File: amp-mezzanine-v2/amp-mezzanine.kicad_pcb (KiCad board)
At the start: 4 copper layers, 49 x 54.8 mm, 10 parts, among them J1 CTRL, J2 PWR, J3 ONEWIRE, J4 ONEWIRE

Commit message: Updated mezannine v2
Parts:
- added H2: MountingHole_Pad, MountingHole:MountingHole_3.2mm_M3_Pad_Via, F.Cu at (115.0, 96.0)
- J3, J4: value ONEWIRE -> Conn_01x02_MountingPin
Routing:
- net GND: vias 79 -> 76
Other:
- board text added: "Designer: ${DESIGNER} Reviewer: ${REVIEWER} ${COMPANY}"

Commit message: Updated all boards for production
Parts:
- removed A100: R, Jumper:SolderJumper-3_P1.3mm_Open_RoundedPad1.0x1.5mm
- removed A101: NC, Jumper:SolderJumper-3_P1.3mm_Open_RoundedPad1.0x1.5mm
- added H3: ~, MountingHole:MountingHole_3.2mm_M3_Pad_Via, F.Cu at (74.2, 49.1)
- added H4: ~, MountingHole:MountingHole_3.2mm_M3_Pad_Via, F.Cu at (115.0, 80.6)
- H1, H2: value MountingHole_Pad -> ~
- J1, J2: footprint Connector_Molex:Molex_PicoBlade_53261-0971_1x09-1MP_P1.25mm_Horizontal -> Connector_Molex:Molex_PicoBlade_53261-1071_1x10-1MP_P1.25mm_Horizontal
- J3, J4: value Conn_01x02_MountingPin -> ONEWIRE
- moved H2 46.9 mm to (115.0, 49.1)
- moved H1 15.4 mm to (74.2, 80.6)
- moved J1 4.34 mm to (94.7, 91.7)
- moved R1 3.64 mm to (91.9, 86.4)
- moved R2 3.64 mm to (91.9, 84.4)
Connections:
- J1 pad 2: /SDA -> /A1
- J1 pad 4: /CTRL_D -> /SDA
- J1 pad 5: /CTRL_C -> /CTRL_D
- J1 pad 6: /CTRL_B -> /CTRL_C
- J1 pad 7: /CTRL_A -> /CTRL_B
- J1 pad 8: /EN -> /CTRL_A
- J1 pad 9: +3V3 -> /EN
- J2 pad 5: unconnected-(J2-Pin_5-Pad5) -> Vdrive
- R1 pad 1: /SDA -> /SCL
- R2 pad 1: /SCL -> /SDA
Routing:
- net /CTRL_D: track 25.8 -> 11.2 mm
- net /CTRL_C: track 25.4 -> 10.8 mm
- net /CTRL_B: track 25.0 -> 11.0 mm
- net /CTRL_A: track 24.6 -> 11.3 mm
- net /SCL: track 18.3 -> 11.8 mm
- net /SDA: track 16.4 -> 11.9 mm, vias 2 -> 0
- net +3V3: track 21.4 -> 17.3 mm
- net /EN: track 31.1 -> 28.1 mm
- net /A1: track 13.2 -> 11.4 mm, vias 3 -> 0
- net GND: vias 76 -> 66
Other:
- board size 49 x 54.8 mm -> 49 x 50 mm
- board text added: "PIC-D HTR MZN V2 Rev.${BOARD_REV}"

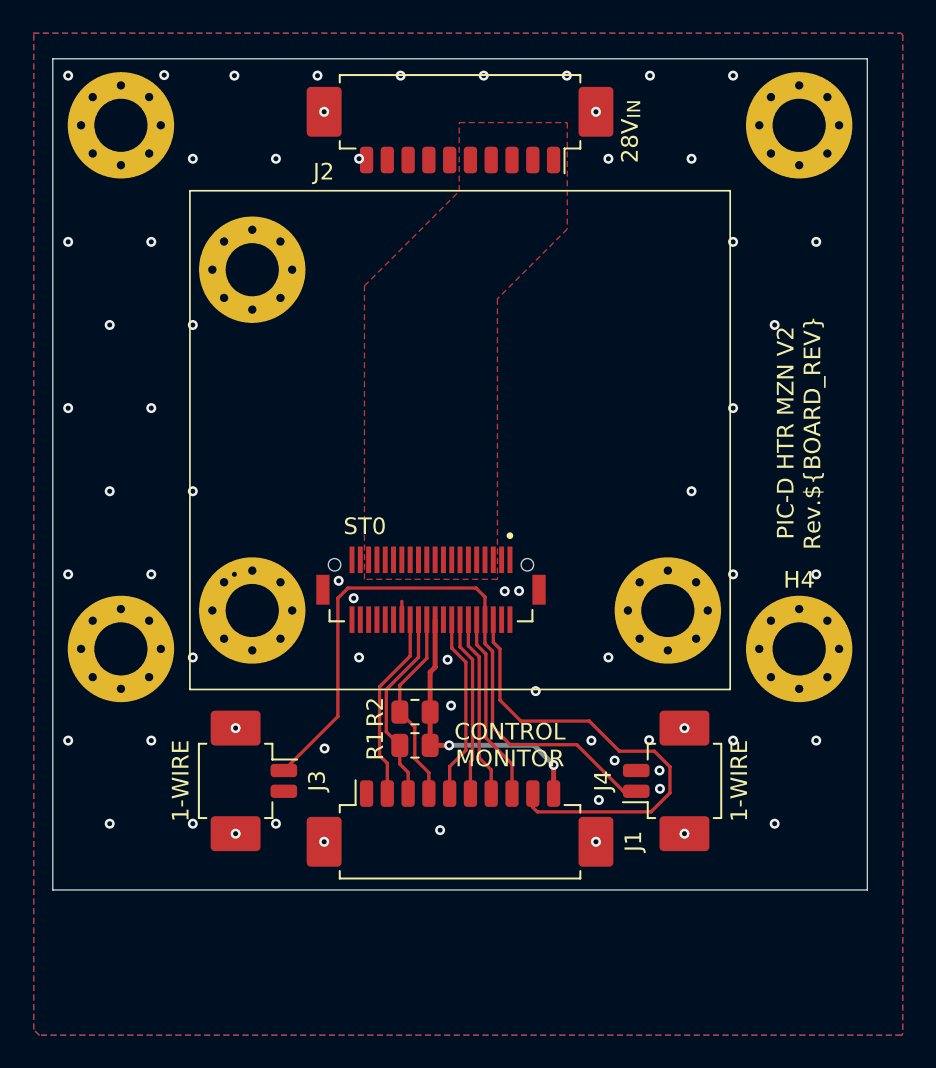
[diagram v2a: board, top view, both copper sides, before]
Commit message: Updated mezzanine v2 with Jason & Joe's comments
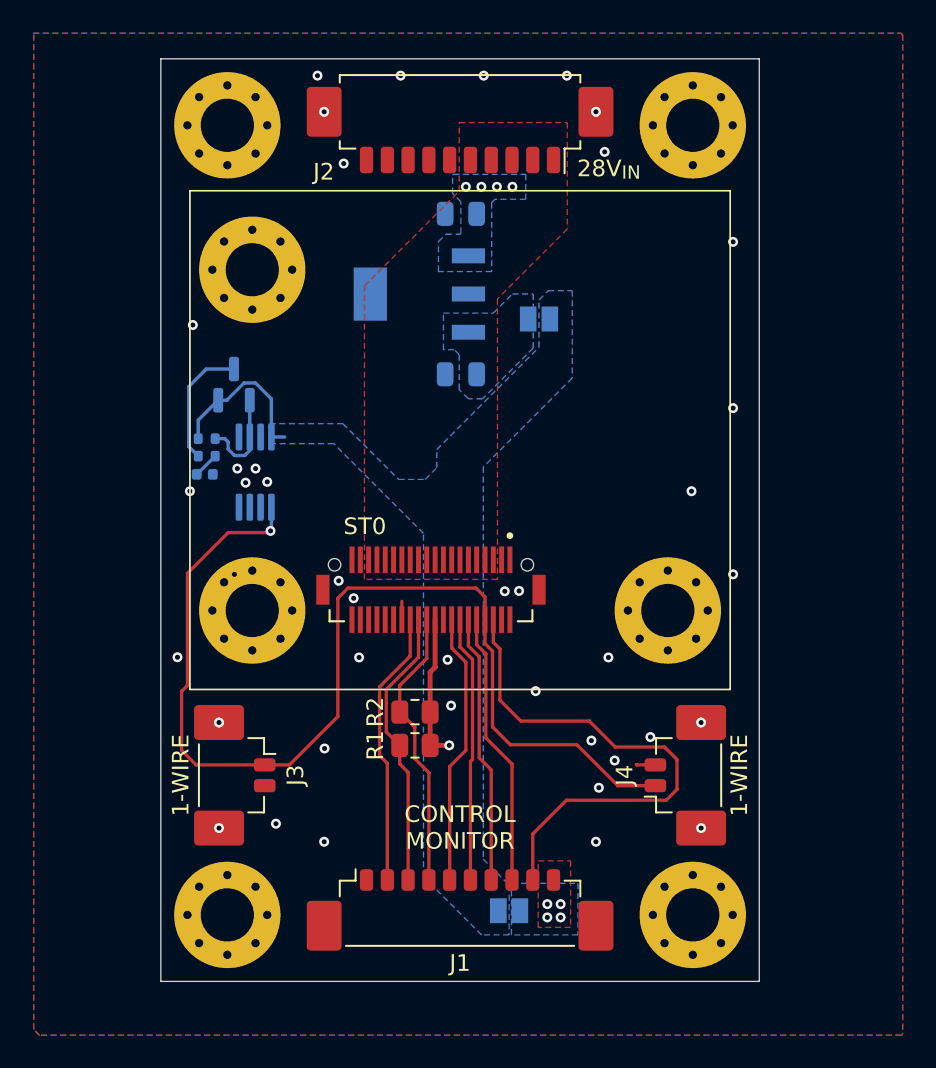
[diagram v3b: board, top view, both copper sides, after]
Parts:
- added C1: 2.2u, Capacitor_SMD:C_0805_2012Metric, B.Cu at (94.7, 54.4)
- added C3: 4.7u, Capacitor_SMD:C_0805_2012Metric, B.Cu at (94.7, 64.0)
- added D1: LED, LED_SMD:LED_0402_1005Metric, B.Cu at (79.3, 70.1)
- added JP1: 3V3_LDO, Jumper:SolderJumper-2_P1.3mm_Open_Pad1.0x1.5mm, B.Cu at (99.4, 60.7)
- added JP2: 3V3_EXT, Jumper:SolderJumper-2_P1.3mm_Open_Pad1.0x1.5mm, B.Cu at (97.6, 96.3)
- added Q1: BSS84, Package_TO_SOT_SMD:SOT-23, B.Cu at (81.0, 64.7)
- added R3: 100k, Resistor_SMD:R_0402_1005Metric, B.Cu at (79.4, 67.9)
- added R4: 1k, Resistor_SMD:R_0402_1005Metric, B.Cu at (79.4, 69.0)
- added U1: DS28EA00, Package_SO:MSOP-8_3x3mm_P0.65mm, B.Cu at (82.3, 69.9)
- added U2: BD433M2FP3-CE2, project_footprints:SOT230P700X180-4N, B.Cu at (92.2, 59.2)
- J1: footprint Connector_Molex:Molex_PicoBlade_53261-1071_1x10-1MP_P1.25mm_Horizontal -> Connector_Molex:Molex_PicoBlade_53398-1071_1x10-1MP_P1.25mm_Vertical
- J3, J4: footprint Connector_Molex:Molex_PicoBlade_53261-0271_1x02-1MP_P1.25mm_Horizontal -> Connector_Molex:Molex_PicoBlade_53398-0271_1x02-1MP_P1.25mm_Vertical
- moved H1 17.2 mm to (80.7, 96.6)
- moved H4 17.2 mm to (108.7, 96.6)
- moved H3 6.40 mm to (80.7, 49.1)
- moved H2 6.40 mm to (108.7, 49.1)
- moved J1 4.05 mm to (94.7, 95.7)
- moved J3 0.34 mm to (81.7, 88.2)
- moved J4 0.34 mm to (107.7, 88.2)
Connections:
- J1 pad 10: +3V3 -> /3V3_IN
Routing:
- net /ONEWIRE: track 39.3 -> 65.0 mm, vias 0 -> 1
- net Net-(Q1-D): track 0.00 -> 7.65 mm
- net /LED_CTRL: track 0.00 -> 5.90 mm
- net /CTRL_B: track 11.0 -> 16.2 mm
- net /CTRL_D: track 11.2 -> 16.4 mm
- net /CTRL_C: track 10.8 -> 16.0 mm
- net /CTRL_A: track 11.3 -> 16.5 mm
- net /A1: track 11.4 -> 16.6 mm
- net /SDA: track 11.9 -> 17.1 mm
- net /SCL: track 11.8 -> 17.0 mm
- net /EN: track 28.1 -> 31.5 mm
- net Net-(D1-A): track 0.00 -> 1.70 mm
- net +3V3: track 17.3 -> 18.8 mm, vias 2 -> 1
- net GND: track 1.10 -> 2.26 mm, vias 66 -> 41
- net Vdrive: vias 0 -> 4
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- added copper zone on B.Cu, net +3V3
- added copper zone on B.Cu, net /3V3_IN
- added copper zone on F.Cu, net /3V3_IN
- added copper zone on B.Cu, net /3V3_LDO
- added copper zone on B.Cu, net Vdrive
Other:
- board size 49 x 50 mm -> 36 x 55.5 mm
- board text added: "3V3_EXT"
- board text added: "3V3_INT -> Internal LDO 3V3_EXT -> External DAC board"
- board text added: "3V3_LDO"
- board text added: "Temperature Sensor"
- board text removed: "PIC-D HTR MZN V2 Rev.${BOARD_REV}"

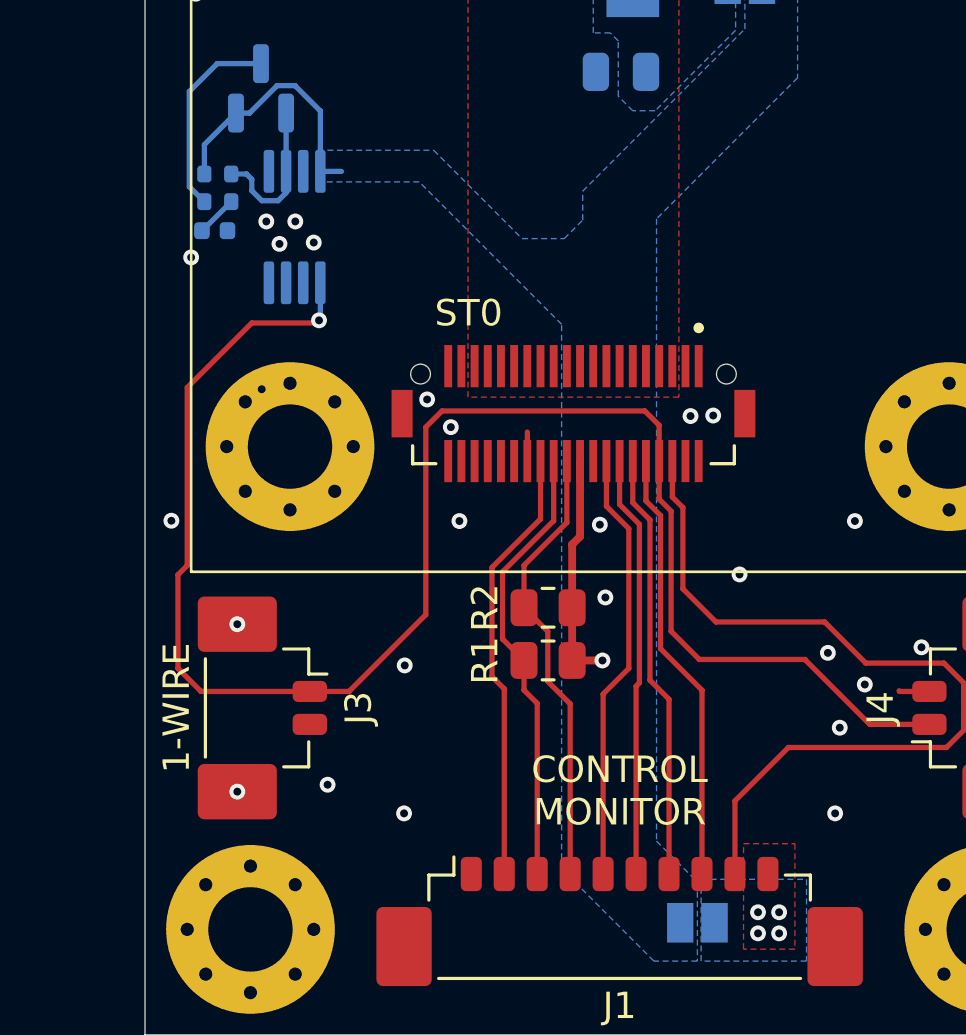
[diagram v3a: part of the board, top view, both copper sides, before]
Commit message: Updated amp-mezzanine: added test points
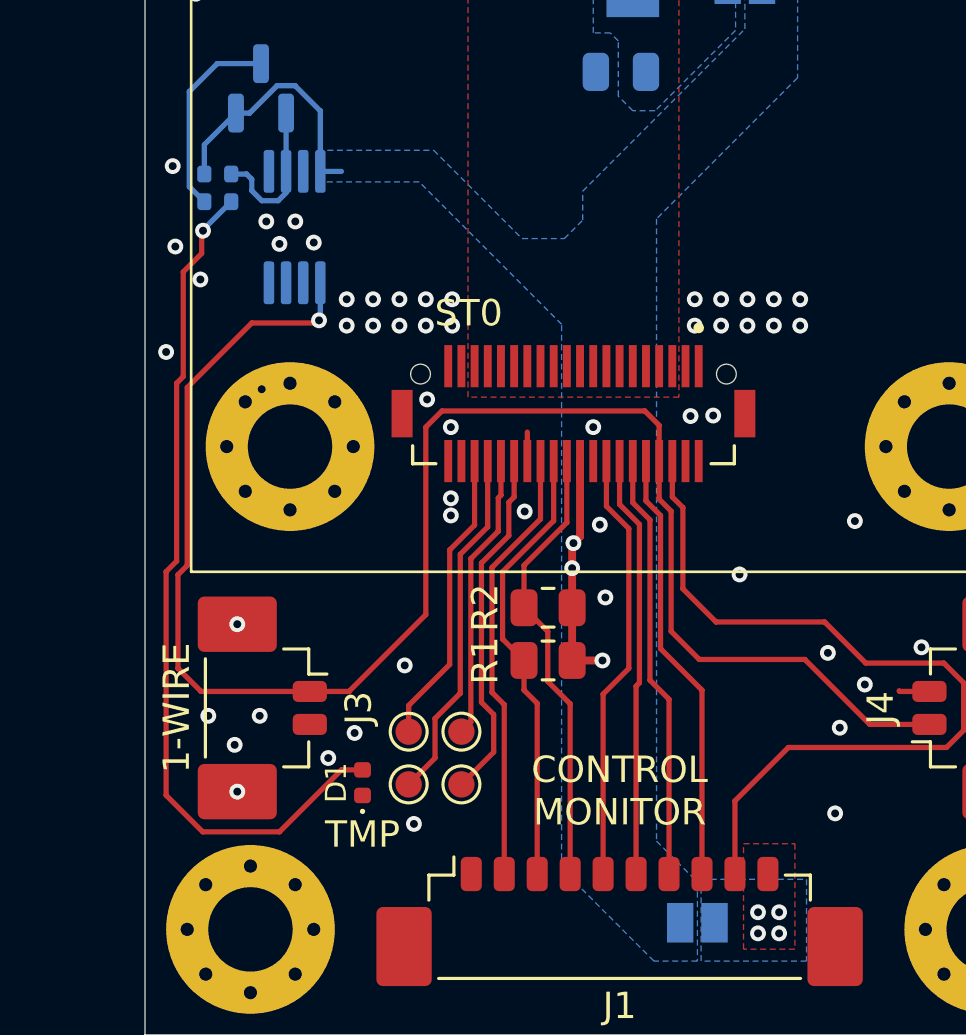
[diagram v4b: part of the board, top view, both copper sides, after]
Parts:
- added TP1: ST_A, TestPoint:TestPoint_Pad_D1.0mm, F.Cu at (88.7, 91.1)
- added TP2: ST_B, TestPoint:TestPoint_Pad_D1.0mm, F.Cu at (88.7, 89.1)
- added TP3: ST_C, TestPoint:TestPoint_Pad_D1.0mm, F.Cu at (86.7, 91.1)
- added TP4: ST_D, TestPoint:TestPoint_Pad_D1.0mm, F.Cu at (86.7, 89.1)
- D1: moved to F.Cu
- moved D1 21.7 mm to (84.9, 91.0), turned to 90 degrees
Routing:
- net Net-(D1-A): track 1.70 -> 32.4 mm, vias 0 -> 1
- net /STAT_C: track 0.00 -> 13.5 mm
- net /STAT_A: track 0.00 -> 13.5 mm
- net /STAT_D: track 0.00 -> 11.3 mm
- net /STAT_B: track 0.00 -> 10.9 mm
- net GND: vias 41 -> 70
- net +3V3: vias 1 -> 3
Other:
- board text added: "AMPHENOL-10132797-045100LF"
- board text added: "CLOSED"
- board text added: "OPEN"
- board text added: "TMP"

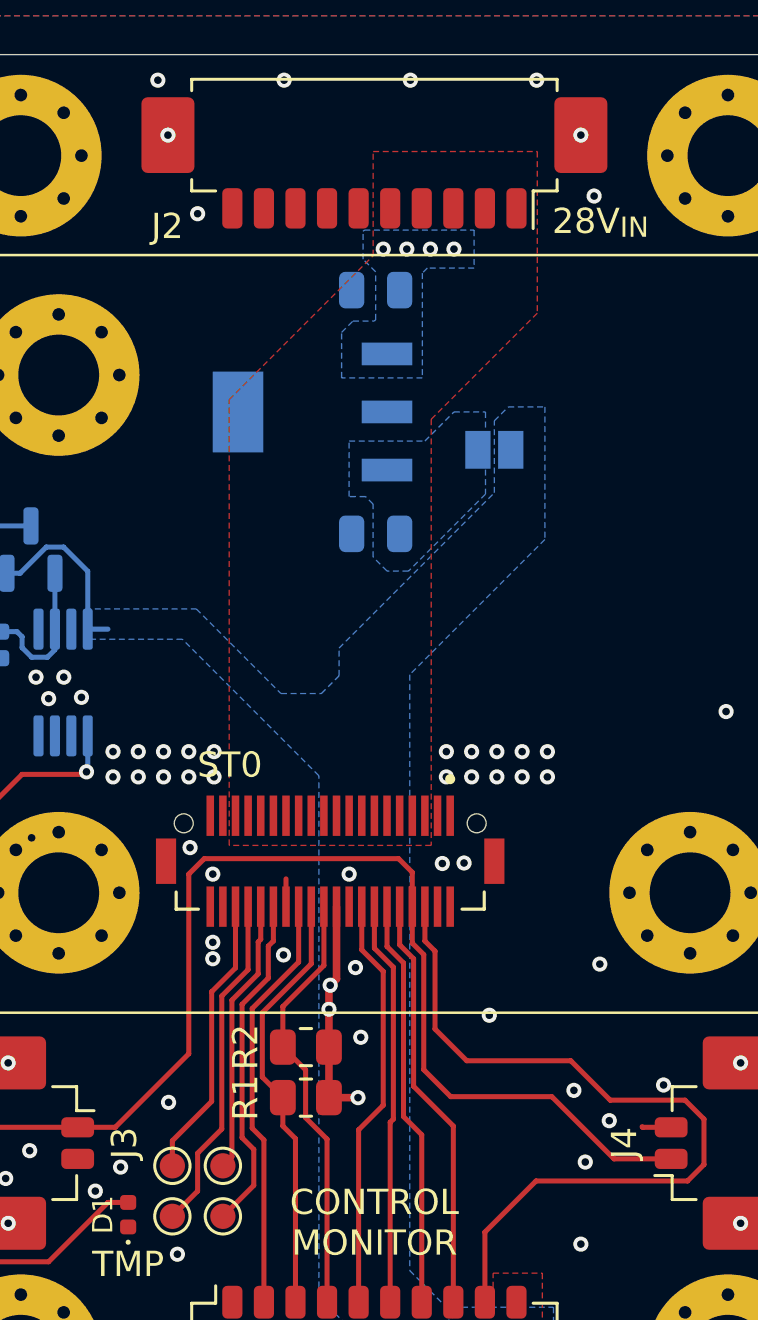
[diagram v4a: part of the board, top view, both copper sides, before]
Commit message: Added part numbers
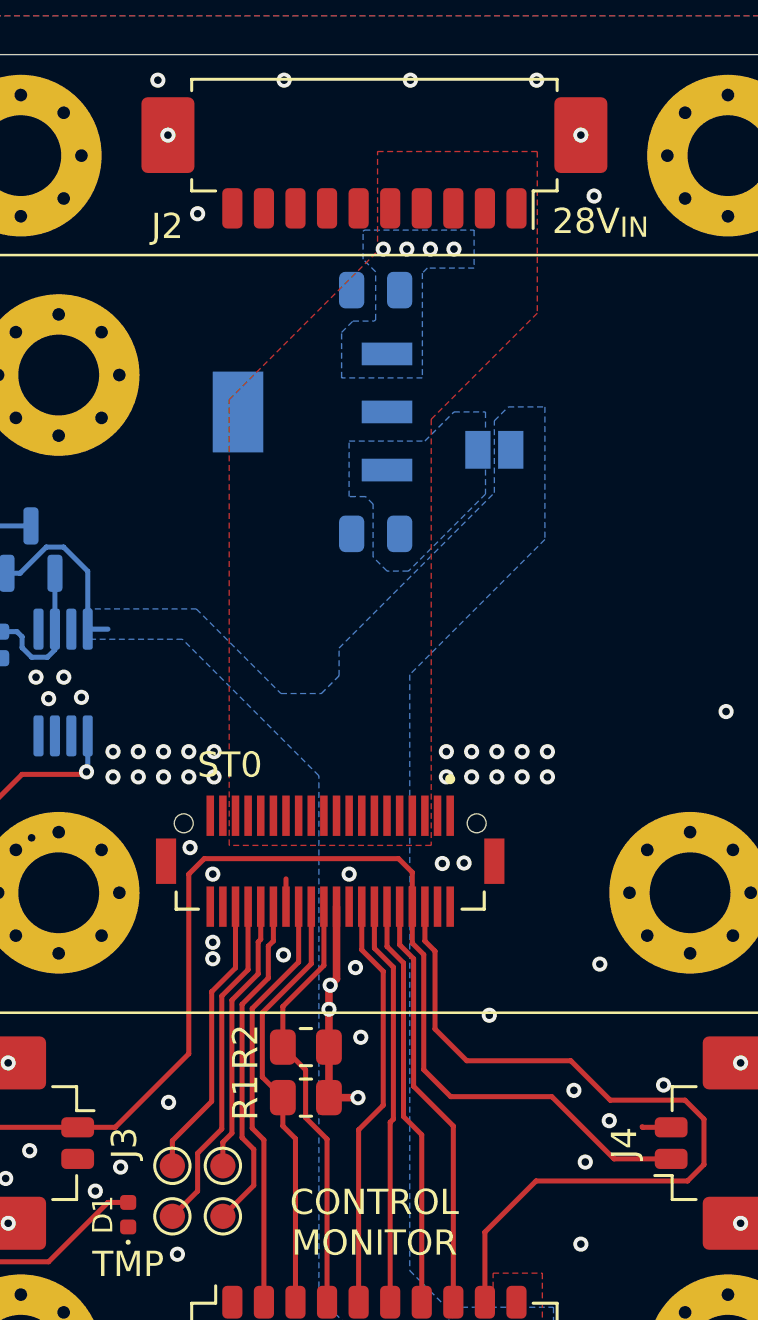
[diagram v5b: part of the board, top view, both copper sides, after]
